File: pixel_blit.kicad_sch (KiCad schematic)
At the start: 39 parts, among them J37 Conn_01x03_Pin, SW1 K2-1808SN-A4SW, U1 RP2350B_C42415655, U2 W25Q128JVSIQTR

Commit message: Convert to KiCad 10 format
Upgrade the schematics, board and project symbol/footprint libraries with
kicad-cli 10.0.1. The netlist is unchanged (222 nets, 760 pins, 214
components) and ERC/DRC match the KiCad 9 results.

The board used parts from the EasyEDA and PCM_JLCPCB libraries, which were
only in the KiCad 9 global tables on one machine. Copy the parts it uses into
the project and add project table entries under the same nicknames, so no
references change. Clear the PCB's Datasheet "~" placeholders, which
KiCad 10 reports as parity mismatches with the schematic's empty fields.
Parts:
- L1, X1: value ~ -> (none)

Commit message: Replace LVDS with RM2 Wi-Fi, add PSRAM, remove display header
- Remove the LVDS transceivers, RJ45s and their protection and termination.
  The sheet becomes wireless.kicad_sch with a Raspberry Pi RM2 (U9) on
  GPIO 32 (WL_ON), 33 (CS), 34 (DATA, via 470R and 10k as on Pico 2 W) and
  35 (CLK), reusing the routed LVDS traces.
- RM2 sits at the left edge with its antenna flush, away from the CPU and
  flash. The footprint carries the datasheet's 35.5 x 18.5 mm RF keep-out
  on every copper layer; side pads moved out 0.5 mm to match datasheet
  Figure 6. The In2 +3V3 trunk moved from x=54.15 to x=60.5 to clear it.
- Add an APS6404L 8 MB QSPI PSRAM (U10) directly under the flash, sharing
  its bus, with CS on GPIO 47 (XIP_CS1) and a 10k pull-up so it stays
  deselected while the bootrom reads flash.
- Remove the front-panel header J39 and its copper; GPIO 40, 41, 43, 45
  and 46 are now no-connects.
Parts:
- added C45: 100nF, PixelBlit:C_0402, symbol PixelBlit:0402,100nF
- added R62: 10kΩ, PixelBlit:R_0402, symbol PixelBlit:0402,10kΩ
- added U10: APS6404L-3SQR-SN, JLCImport:APS6404L-3SQR-SN_C5333729, symbol JLCImport:APS6404L-3SQR-SN_C5333729
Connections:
- net +3V3: now also C45.1, R62.1, U10.8 (VDD)
- net GND: now also C45.2, U10.4 (VSS)
- net QSPI_SD3: now reaches U1.70 (QSPI_SD3), U2.7 (IO3)
- net QSPI_SD3: now also U10.7 (SIO[3])
- net QSPI_SCLK: now reaches U1.71 (QSPI_SCLK), U2.6 (CLK)
- net QSPI_SCLK: now also U10.6 (SCLK)
- net QSPI_SD0: now reaches U1.72 (QSPI_SD0), U2.5 (DI)
- net QSPI_SD0: now also U10.5 (SI/SIO[0])
- net QSPI_SD2: now reaches U1.73 (QSPI_SD2), U2.3 (IO2)
- net QSPI_SD2: now also U10.3 (SIO[2])
- net QSPI_SD1: now reaches U1.74 (QSPI_SD1), U2.2 (DO)
- net QSPI_SD1: now also U10.2 (SO/SIO[1])
- net BAK: no longer names the net of U1.49 (GPIO40_ADC0)
- net DATA_IN_EN: no longer names the net of U1.55 (GPIO44_ADC4)
- net DISP_SCL renamed PSRAM_CS
- net PSRAM_CS: now also R62.2, U10.1 (CE#)
- net DISP_SDA: no longer names the net of U1.57 (GPIO46_ADC6)
- net HS_DATA0 renamed WL_CLK
- net HS_DATA1 renamed WL_DATA
- net HS_DATA2 renamed WL_CS
- net HS_DATA3 renamed WL_ON
- net PSH: no longer names the net of U1.52 (GPIO41_ADC1)
- net TRA: no longer names the net of U1.56 (GPIO45_ADC5)
- net TRB: no longer names the net of U1.54 (GPIO43_ADC3)
- no-connect marks 2 -> 8
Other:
- sheet Communications renamed Wireless
- sheet Wireless: file communications.kicad_sch -> wireless.kicad_sch
- note added: "CS on GPIO 47 = XIP_CS1 (QMI chip select 1). R62 holds it high at reset, when GPIO pulls default low, so the PSRAM stays off the bus while the bootrom reads flash."
- note added: "PSRAM (8 MB QSPI, shares the flash bus)"

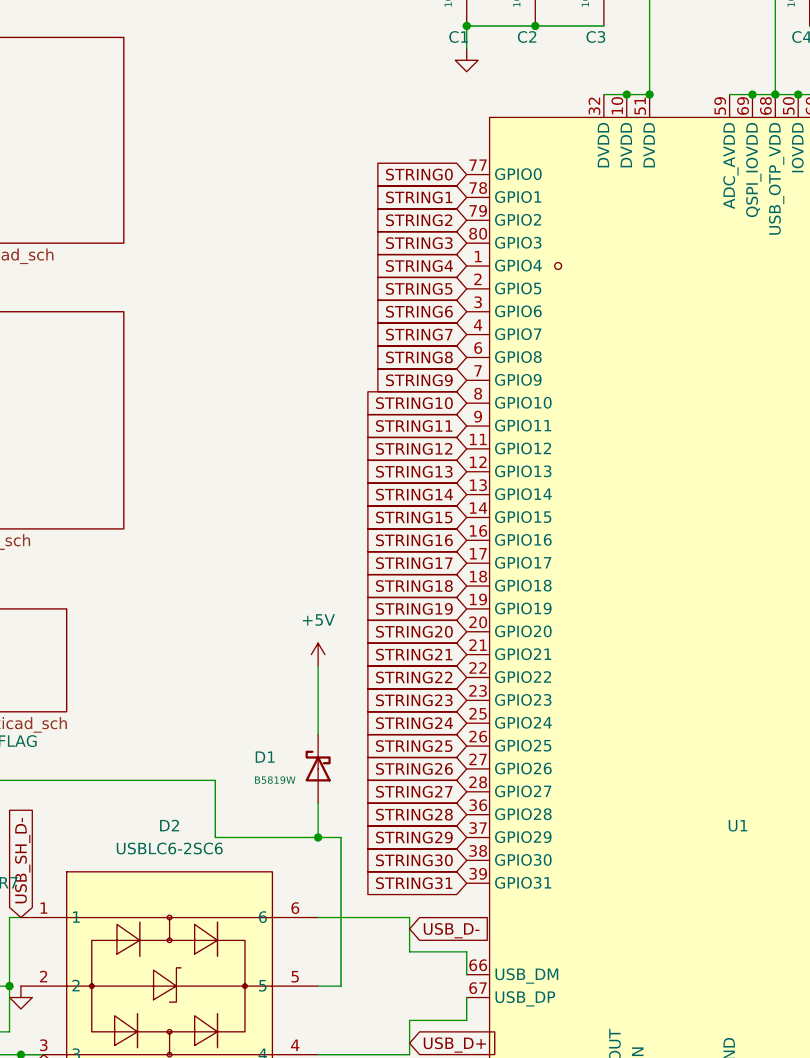
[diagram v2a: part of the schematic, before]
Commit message: Zone silkscreen, 30V port PTCs, string renumbering
- Port PTCs: LUTE 1812L300/30GR (C48985875) imported via jlcimport, pins
  redrawn to match the old symbol; pads unchanged.
- Nets STRINGn/Sn_OUT renumbered by zone (Z1 S0-7 .. Z4 S24-31).
- Silkscreen: S<n>.Z<z> labels, + Zn - on input terminals, zone borders
  following the pours, zone key with voltage write-in, 5-24VDC/VIN labels.
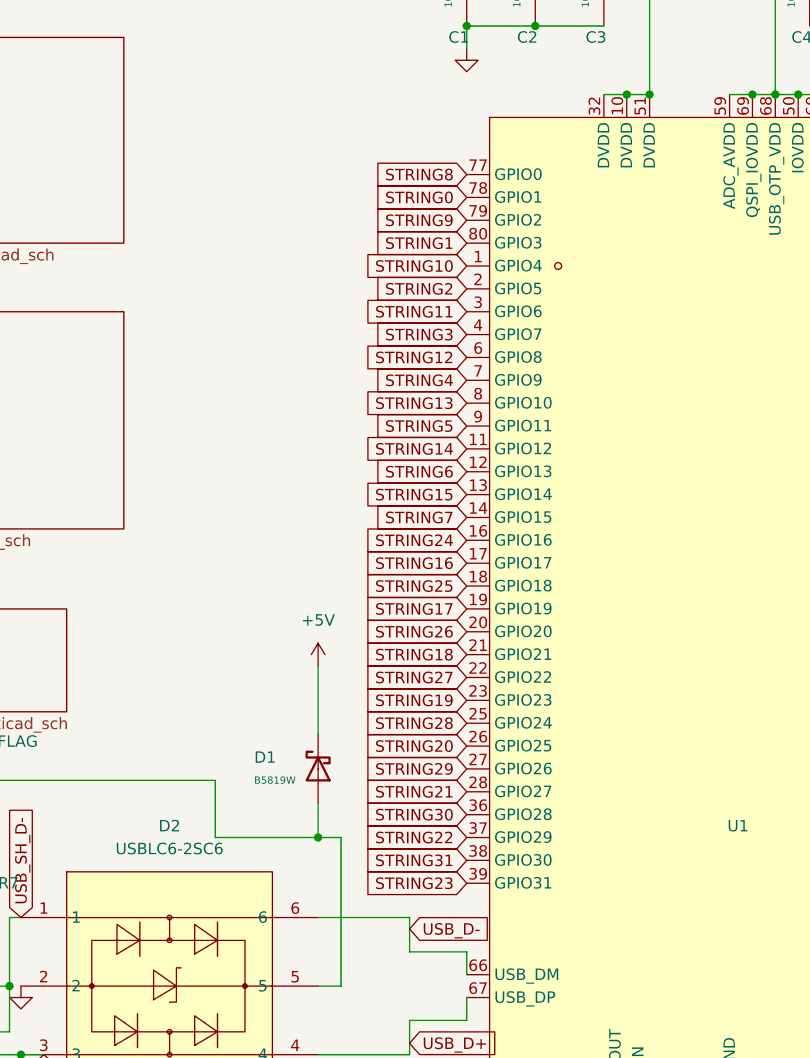
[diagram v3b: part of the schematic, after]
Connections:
- net STRING0: now also U1.78 (GPIO1); no longer U1.77 (GPIO0)
- net STRING1: now also U1.80 (GPIO3); no longer U1.78 (GPIO1)
- net STRING10: now also U1.1 (GPIO4); no longer U1.8 (GPIO10)
- net STRING11: now also U1.3 (GPIO6); no longer U1.9 (GPIO11)
- net STRING12: now also U1.6 (GPIO8); no longer U1.11 (GPIO12)
- net STRING13: now also U1.8 (GPIO10); no longer U1.12 (GPIO13)
- net STRING14: now also U1.11 (GPIO12); no longer U1.13 (GPIO14)
- net STRING15: now also U1.13 (GPIO14); no longer U1.14 (GPIO15)
- net STRING16: now also U1.17 (GPIO17); no longer U1.16 (GPIO16)
- net STRING17: now also U1.19 (GPIO19); no longer U1.17 (GPIO17)
- net STRING18: now also U1.21 (GPIO21); no longer U1.18 (GPIO18)
- net STRING19: now also U1.23 (GPIO23); no longer U1.19 (GPIO19)
- net STRING2: now also U1.2 (GPIO5); no longer U1.79 (GPIO2)
- net STRING20: now also U1.26 (GPIO25); no longer U1.20 (GPIO20)
- net STRING21: now also U1.28 (GPIO27); no longer U1.21 (GPIO21)
- net STRING22: now also U1.37 (GPIO29); no longer U1.22 (GPIO22)
- net STRING23: now also U1.39 (GPIO31); no longer U1.23 (GPIO23)
- net STRING24: now also U1.16 (GPIO16); no longer U1.25 (GPIO24)
- net STRING25: now also U1.18 (GPIO18); no longer U1.26 (GPIO25)
- net STRING26: now also U1.20 (GPIO20); no longer U1.27 (GPIO26)
- net STRING27: now also U1.22 (GPIO22); no longer U1.28 (GPIO27)
- net STRING28: now also U1.25 (GPIO24); no longer U1.36 (GPIO28)
- net STRING29: now also U1.27 (GPIO26); no longer U1.37 (GPIO29)
- net STRING3: now also U1.4 (GPIO7); no longer U1.80 (GPIO3)
- net STRING30: now also U1.36 (GPIO28); no longer U1.38 (GPIO30)
- net STRING31: now also U1.38 (GPIO30); no longer U1.39 (GPIO31)
- net STRING4: now also U1.7 (GPIO9); no longer U1.1 (GPIO4)
- net STRING5: now also U1.9 (GPIO11); no longer U1.2 (GPIO5)
- net STRING6: now also U1.12 (GPIO13); no longer U1.3 (GPIO6)
- net STRING7: now also U1.14 (GPIO15); no longer U1.4 (GPIO7)
- net STRING8: now also U1.77 (GPIO0); no longer U1.6 (GPIO8)
- net STRING9: now also U1.79 (GPIO2); no longer U1.7 (GPIO9)
